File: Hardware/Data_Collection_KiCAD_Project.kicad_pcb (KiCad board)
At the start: 4 copper layers, 80 x 93.2 mm, 67 parts, among them IC1 STM32L562VET6Q, J1 10118192-0001LF, J2 Conn_Coaxial, J3 L717SDC37P1ACH4F, J4 I2C1 Debug, J5 EXT I2c Debug, J6 UART Debug, J7 SPI 1 Debug, J8 Ext SPI Debug, Q1 SI1040X-T1-GE3, U1 LM317T, U2 KX134-1211, U3 MCP9808_MSOP, U4 MAX-8Q, U5 USBLC6-2SC6, U6 W25Q32JVSS, U7 MS5607-02BA, U8 BNO055, Y1 32MHz, Y2 32.768kHz

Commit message: finished routing
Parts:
- removed C17, C3, C6: 100nF, Capacitor_SMD:C_0603_1608Metric_Pad1.08x0.95mm_HandSolder
- removed J5: EXT I2c Debug, Connector_PinHeader_2.54mm:PinHeader_1x02_P2.54mm_Vertical
- removed J8: Ext SPI Debug, Connector_PinHeader_2.54mm:PinHeader_1x03_P2.54mm_Vertical
- removed TP14, TP15, TP16: Debug Pad, TestPoint:TestPoint_Pad_D1.0mm
- moved R10 167.3 mm to (152.0, 118.5), turned to 270 degrees
- moved R11 165.5 mm to (152.0, 112.7), turned to 90 degrees
- moved D2 160.4 mm to (155.0, 118.5), turned to 270 degrees
- moved D3 157.6 mm to (155.0, 112.7)
- moved J6 143.5 mm to (116.9, 112.4), turned to 90 degrees
- moved C11 135.8 mm to (107.9, 77.6), turned to 225 degrees
- moved J4 126.1 mm to (102.2, 92.8)
- moved C4 115.8 mm to (127.8, 111.6), turned to 45 degrees
- moved C8 114.9 mm to (126.5, 110.2), turned to 45 degrees
- moved C10 110.9 mm to (97.0, 72.3), turned to 90 degrees
- moved C7 106.3 mm to (123.8, 65.0), turned to 315 degrees
- moved C24 104.3 mm to (106.6, 76.2), turned to 225 degrees
- moved C12 104.3 mm to (116.2, 88.0), turned to 0 degrees
- moved R8 98.8 mm to (108.3, 86.1)
- moved R9 94.5 mm to (110.4, 87.0), turned to 270 degrees
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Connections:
- IC1 pad 62: Net-(IC1-Pad62) -> (no net)
- IC1 pad 63: Net-(IC1-Pad63) -> (no net)
- IC1 pad 64: Net-(IC1-Pad64) -> (no net)
- R10 pad 1: Net-(IC1-Pad2) -> Net-(IC1-Pad37)
- R11 pad 1: Net-(IC1-Pad37) -> Net-(IC1-Pad2)
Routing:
- net GND: track 84.9 -> 184.7 mm, vias 7 -> 14
- net Net-(IC1-Pad37): track 0.00 -> 77.2 mm, vias 0 -> 2
- net Net-(IC1-Pad2): track 0.00 -> 72.6 mm, vias 0 -> 2
- net +3V3: track 55.4 -> 124.8 mm, vias 4 -> 8
- net /37 Pin DSUB Bus/Dsub_5v: track 0.00 -> 64.1 mm
- net +5V: track 29.4 -> 86.6 mm
- net /USART1_RX: track 0.00 -> 49.4 mm, vias 0 -> 2
- net /SWCLK: track 0.00 -> 48.0 mm, vias 0 -> 1
- net /USART1_TX: track 0.00 -> 45.5 mm, vias 0 -> 2
- net /SWDIO: track 0.00 -> 44.3 mm, vias 0 -> 1
- net /NRST: track 0.00 -> 38.8 mm, vias 0 -> 1
- net /I2C1_SCL: track 47.8 -> 78.8 mm, vias 2 -> 3
- net /I2C1_SDA: track 52.6 -> 82.3 mm, vias 4 -> 5
- net /EXT_SDA: track 0.00 -> 27.5 mm
- net /SPI2_MOSI: track 0.00 -> 25.2 mm, vias 0 -> 2
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
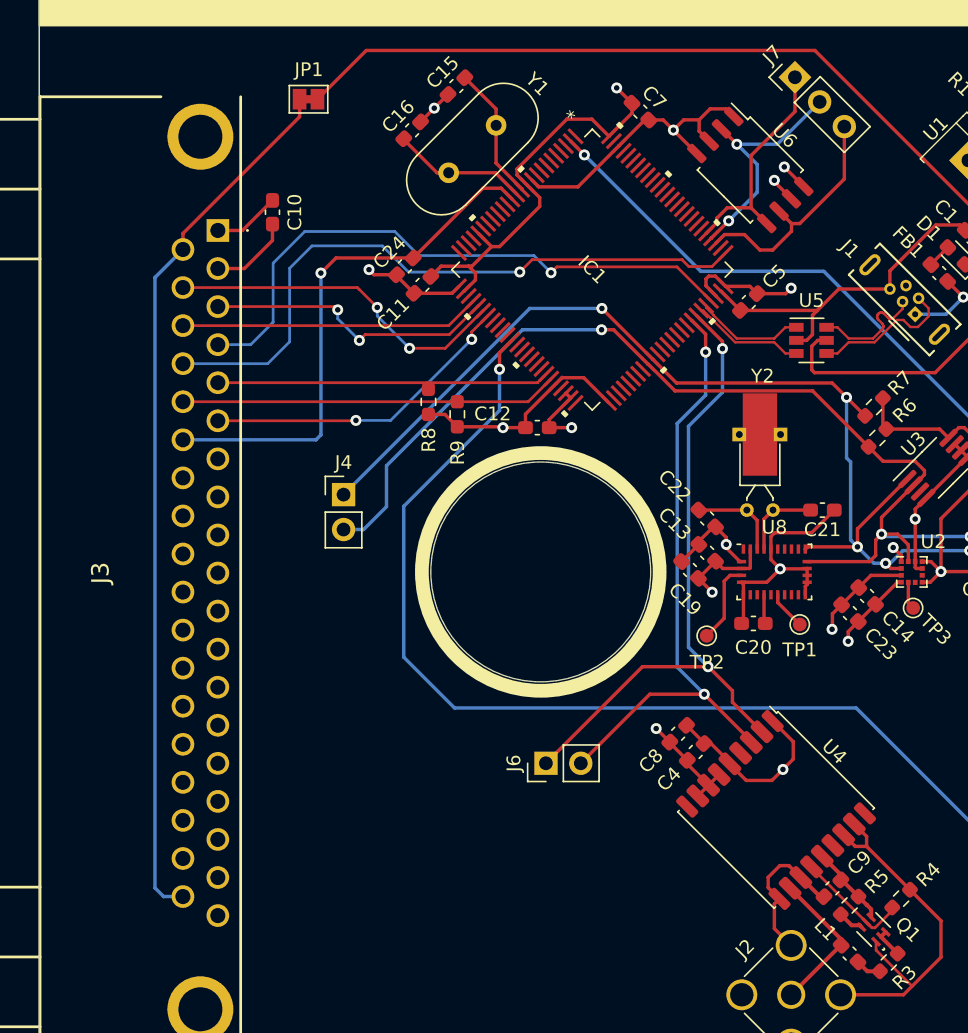
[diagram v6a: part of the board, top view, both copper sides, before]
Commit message: Updated file format to KiCAD v6, replaced voltage regulator
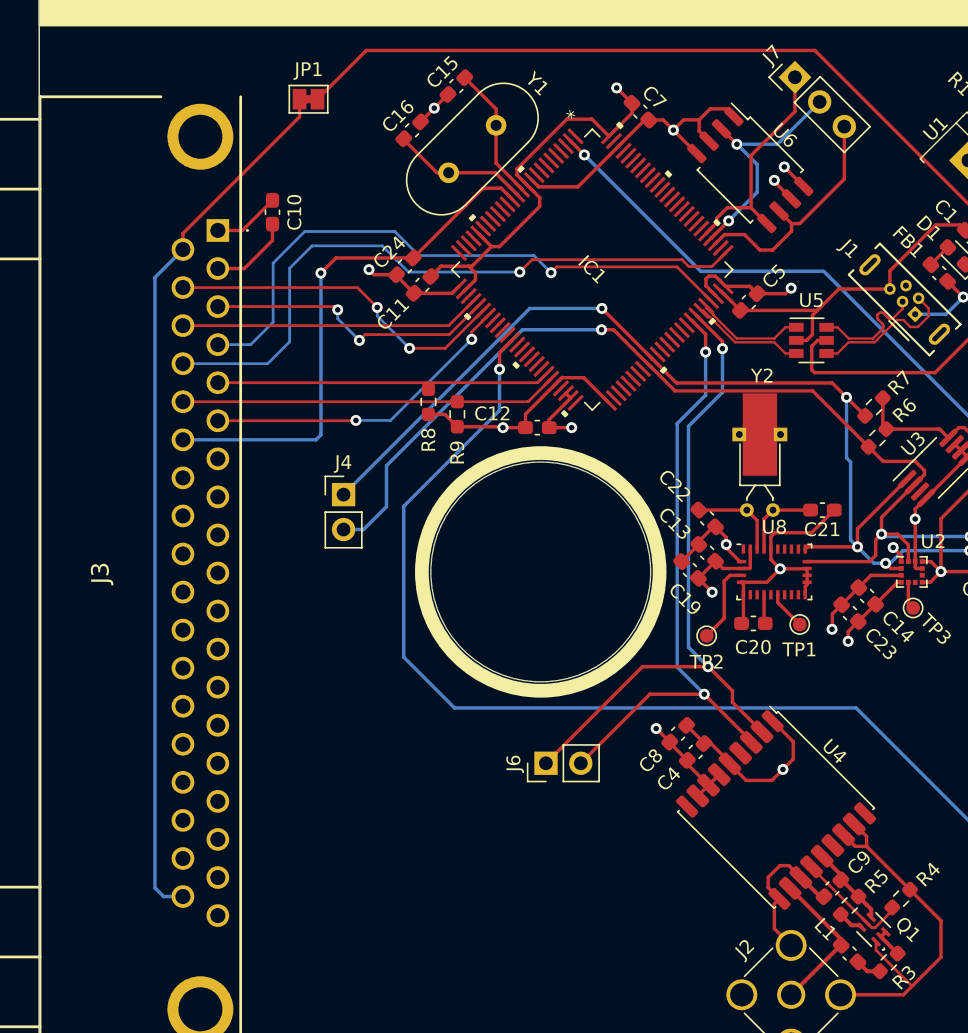
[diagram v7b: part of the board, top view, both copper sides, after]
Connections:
- net /BNO055/~BNO055_BTL renamed /BNO055/~{BNO055_BTL}
- net /BNO055/~BNO055_RESET renamed /BNO055/~{BNO055_RESET}
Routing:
- added copper zone on In2.Cu, net +3V3
- added copper zone on In1.Cu, net GND
- removed copper zone on 3.3V.Cu, net +3V3
- removed copper zone on GND.Cu, net GND
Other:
- net class DIFF_90_USB removed
- net class Default removed
